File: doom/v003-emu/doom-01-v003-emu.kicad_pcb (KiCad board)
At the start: 2 copper layers, 96 x 92 mm, 67 parts, among them Q1 AO3401A, Q2 FS8205A, SW1 TS-1187A-B-A-B, SW2 TS-1187A-B-A-B, SW3 TS-1187A-B-A-B, SW4 TS-1187A-B-A-B, SW5 TS-1187A-B-A-B, SW6 TS-1187A-B-A-B, SW7 TS-1187A-B-A-B, SW8 TS-1187A-B-A-B, SW9 MSK12C02, U1 CH32V003F4P6, U2 APS6404L-3SQR-SN, U3 W25Q128JVSIQ, U4 AP2112K-3.3TRG1, U5 DW01A, U6 BQ24075RGTR

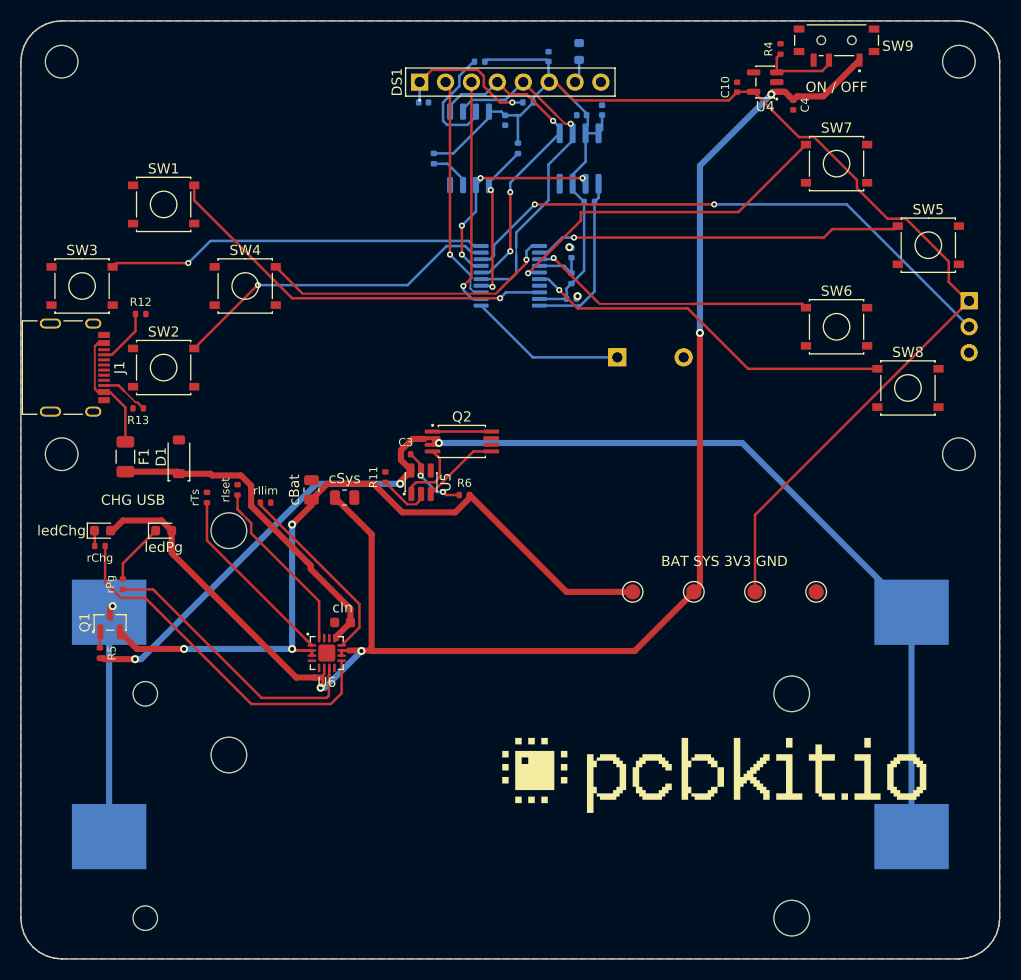
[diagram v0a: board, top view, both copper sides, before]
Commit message: Boards pass check and KiCad 10's DRC again: holes in courtyards, the USB net rename
pcbkit's check now has KiCad 10's pth/npth_inside_courtyard (pcbkit be5b6955), and 13 boards
failed it. KiCad's own DRC (kicad-cli 10) reports the same holes on every one of them.

- Parts that really stand above the holes under them (a screen or a Nano on its sockets, the
  Delta-S02's КМ-6 capacitors flat under its chips, as the factory placed them): a courtyard rule
  for the pair, written to each board's .kicad_dru, so KiCad's DRC agrees.
- Real collisions moved: servo-controller's dial 3 mm up (the Nano's socket pins came out under
  it), c3-pocket's fourth M3 hole from under a cell holder to the top edge's middle, s3-rgb's
  D-pad 2 mm up (a holder's peg came through under the down key).
- v003-emu, c3-pocket, rp2040-tft, rp2350-psram, s3-rgb, teensy41: re-routed for the standard USB
  block's renamed net (usb/raw is usb/vbusIn since pcbkit 2088839e): their tracks still carried
  the old name and shorted the fuse and connector pads.
- p4-touch-7: its board file still had a courtyard for the panel the design gives none (KiCad
  reported 114 courtyard errors); written again.

Measured on the dev host: all 44 registry boards `pcbkit check` complete with 0 errors, and
kicad-cli pcb drc 0 errors on every board.

Claude-Session: https://claude.ai/code/session_018URVYF1YPgyrMNetY9yT1T
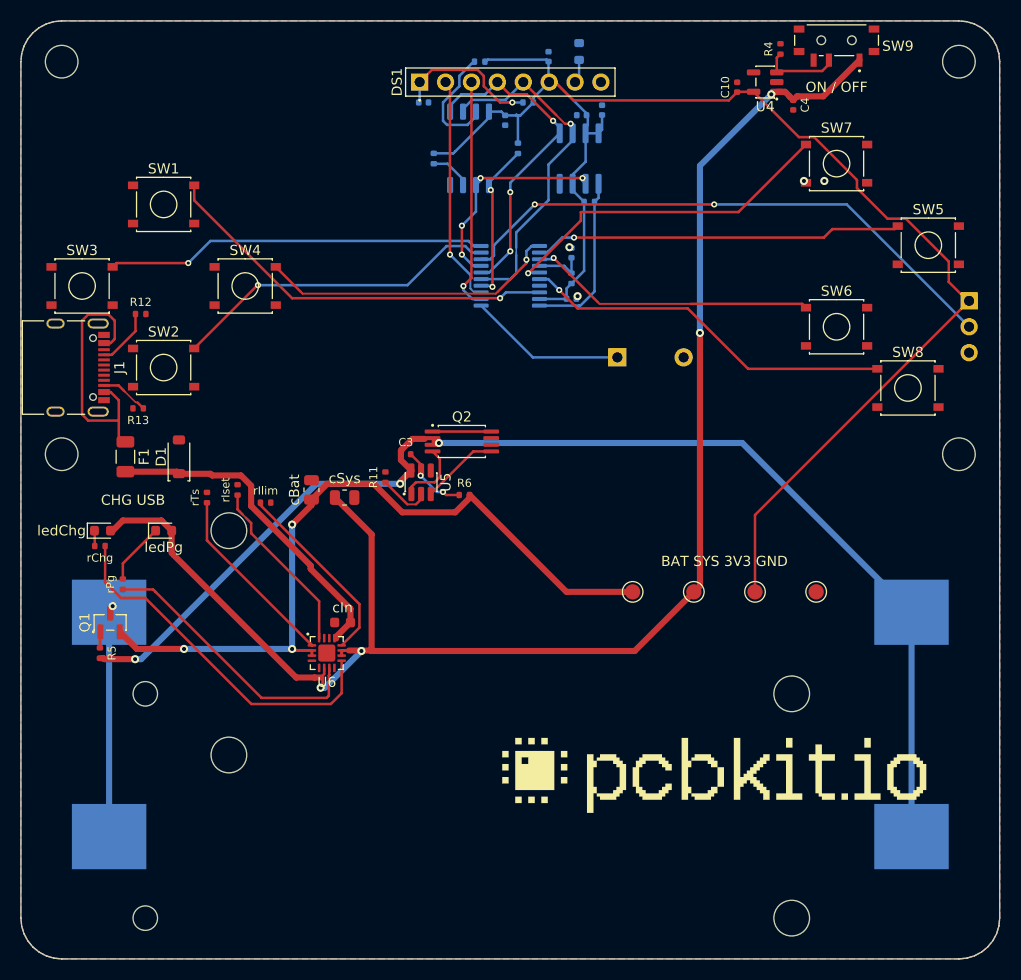
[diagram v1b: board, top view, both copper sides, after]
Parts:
- F1: value PTC 680mA -> PTC 500mA
- H1, H2, H3, H4: value (none) -> MountingHole_3.2mm_M3
- J1: value (none) -> USB4105-GF-A
- J2: value (none) -> PinHeader_1x03_P2.54mm_Vertical
- logo: value (none) -> Logo_PCBKit_pcbkit.io
- tpBat, tpGnd, tpSys, tpV3: value (none) -> TestPoint_Round_D1.5mm
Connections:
- net usb/raw renamed usb/vbusIn
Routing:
- net usb/vbusIn: track 13.5 -> 24.7 mm
- net MISO: track 25.7 -> 22.0 mm
- net RIGHT: track 31.1 -> 29.6 mm
- net SCK: track 34.8 -> 33.4 mm
- net LCD_CS: track 23.7 -> 22.5 mm
- net LCD_BL: track 3.47 -> 2.34 mm
- net LEFT: track 38.4 -> 37.4 mm
- net GND: vias 2 -> 4

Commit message: doom: a resettable fuse per 18650 cell, a 2 % backlight clamp, a 1 A LDO on the S3 boards
The verifier (wiring-parallel-cells) found the two holders of every Doom board directly in parallel:
a cell put in backwards, or one much fuller than the other, drives the other through nothing but
the cells' resistance (about 56-168 A). Each holder's + now reaches BAT_IN through its own 2 A
resettable fuse (Littelfuse 1812L200/16GR, C18198340: 16 V, 100 A interrupting) on new nets
CELL1_P / CELL2_P. Nothing else moved; the boards were re-routed for the new nets.

- s3-rgb: the MT3608 backlight's open-panel clamp was a 28 V 5 % zener (bound 30.0 V against the
  switch's 30 V). It is now two 2 % zeners in series, UDZVTE-1718B + UDZVTE-1710B (27.33-28.56 V;
  LCSC stocks no single 28 V 2 % part). That is under 29.2 V and above the panel's 27.2 V.
- s3-rgb, s3-handheld: TLV75533 (500 mA) -> TLV75733 (1 A, C485517, same DBV pins; sheet from
  SBVS322C), for the ESP32-S3's 500 mA supply peaks (erc-supply-peak).
- c3-pocket, v003-emu: the USB PTC's hold is 750 mA, as the part (nSMD075) is (rating-current).
- pico2-carrier: the CHG/PG LEDs 1.5 mm further from the display's courtyard. rp2350-handheld:
  the logo off the LCD's courtyard and BT1's peg.
- READMEs: the per-cell fuses, the boards already ordered (s3-rgb, JLC W2026102705013253: insert
  the cells one at a time), status and BOM as check and the fab export give them now.

Measured on the dev host (pcbkit 5e0d2cc8): all 11 complete, 0 errors, 0 unrouted. What is left is
erc-rail-name (sent to the verifier as false positives) and full-speed USB pair coupling. The MCU
pins' nets are unchanged on every board, so the firmware and its simulation are unchanged.

Claude-Session: https://claude.ai/code/session_01B3VRfBCg9vAvGVWujVGarr
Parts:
- added F2: PTC 2000mA, Fuse_1812_4532Metric, B.Cu at (115.8, 150.5)
- added F3: PTC 2000mA, Fuse_1812_4532Metric, B.Cu at (110.2, 152.0)
- F1: value PTC 500mA -> PTC 750mA
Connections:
- BT1 pad 2: BAT_IN -> CELL1_P
- BT2 pad 2: BAT_IN -> CELL2_P
- SW1 pad 2: UP -> GND
- SW2 pad 2: DOWN -> GND
- SW3 pad 2: LEFT -> GND
- SW4 pad 2: RIGHT -> GND
- SW5 pad 2: FIRE -> GND
- SW6 pad 2: USE -> GND
- SW7 pad 2: STRAFE -> GND
- SW8 pad 2: MENU -> GND
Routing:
- net CELL1_P: track 0.00 -> 53.8 mm
- net CELL2_P: track 0.00 -> 14.2 mm
- net BAT_IN: track 22.0 -> 18.5 mm

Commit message: boards: 15 boards rebuilt on pcbkit 20ffacdc9 (their pours under the 0.25 mm hole clearance)
Every board checked with main: 17 of 44 failed on hole-clearance (pours filled before fill c6 made
0.25 mm KiCad's hole clearance the default), keepout (holes now sized by the board) or
place-corner. design.run {} on each (placement and routing kept, pours refilled): 15 now complete,
0 errors. Not here: esp32-p4-touch-lcd-7b and p4-touch-7 (a build reroutes their pairs: 21 and 7
unrouted; kept as they were, 2,372 and 919 hole-clearance errors: a refill without a reroute is
needed).

Claude-Session: https://claude.ai/code/session_01BAgp959tApA8aEg85EYgfb
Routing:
- net CELL1_P: track 53.8 -> 39.5 mm, vias 0 -> 2
